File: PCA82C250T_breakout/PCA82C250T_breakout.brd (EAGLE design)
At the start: 36.8 x 17.8 mm, 11 parts, among them J1 RJ11

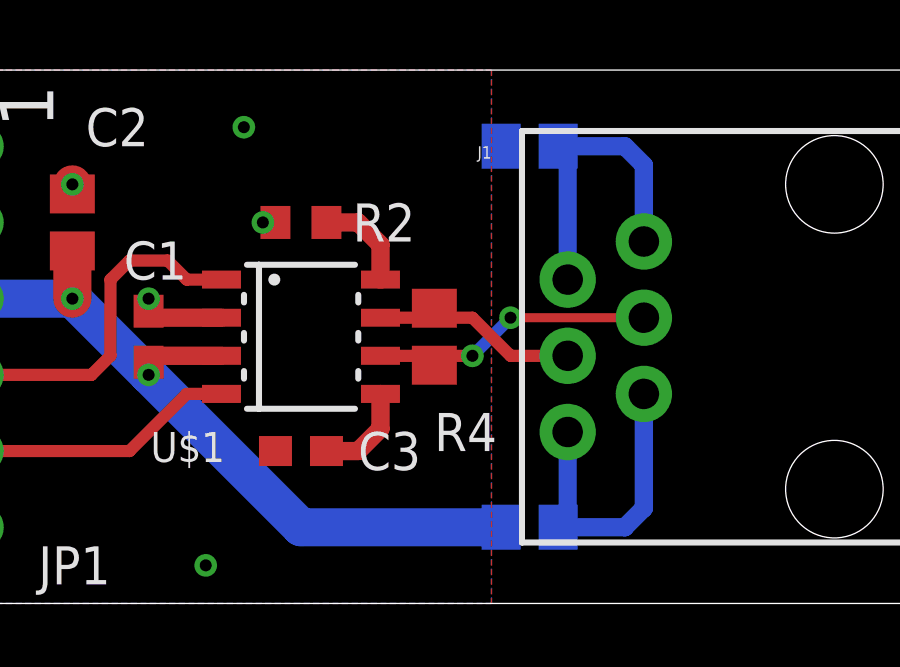
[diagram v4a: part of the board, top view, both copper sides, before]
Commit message: * small modifications and changed pinout
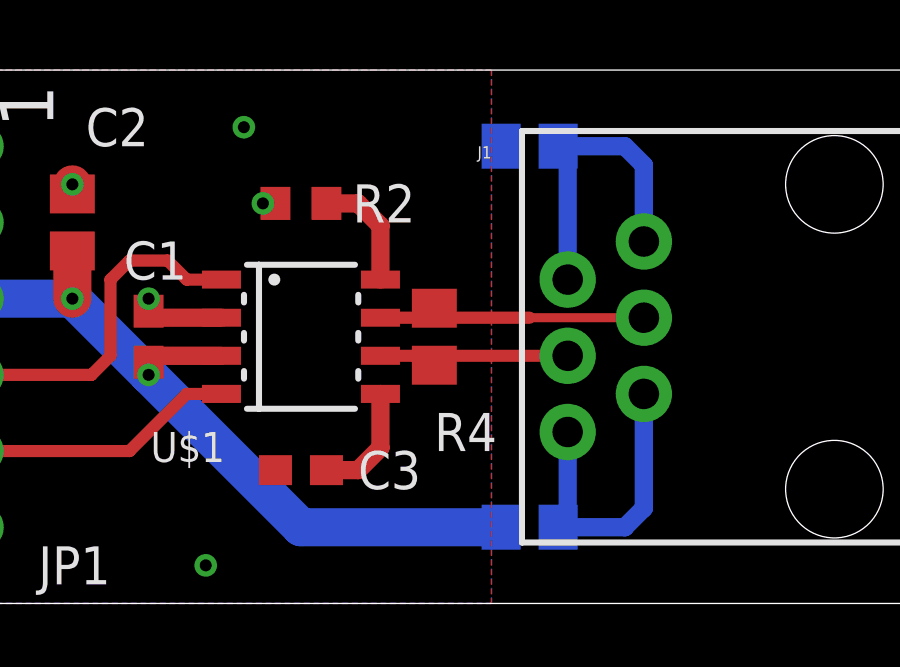
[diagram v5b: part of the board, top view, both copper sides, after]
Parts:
- moved R2 0.64 mm to (14.0, 13.3)
- moved C3 0.63 mm to (14.0, 4.45)
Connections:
- net CANH: now also J1.4; no longer J1.3
- net CANL: now also J1.3; no longer J1.4
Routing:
- net CANL: track 9.62 -> 6.55 mm, vias 2 -> 0
- net CANH: track 7.08 -> 9.04 mm
- net N$5: track 3.27 -> 3.90 mm
- net N$2: track 3.27 -> 3.90 mm
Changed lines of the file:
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@@
 <attribute name="VALUE" x="17.145" y="4.445" size="1.27" layer="28" rot="MR180"/>
 </element>
-<element name="R2" library="SquantorRCL" package="R0603" value="RS" x="13.97" y="12.7" smashed="yes" rot="R180">
-<attribute name="NAME" x="17.78" y="13.335" size="1.27" layer="25" rot="R180"/>
-<attribute name="VALUE" x="17.78" y="15.24" size="1.27" layer="27" rot="R180"/>
+<element name="R2" library="SquantorRCL" package="R0603" value="RS" x="13.97" y="13.335" smashed="yes" rot="R180">
+<attribute name="NAME" x="17.78" y="13.97" size="1.27" layer="25" rot="R180"/>
+<attribute name="VALUE" x="17.78" y="15.875" size="1.27" layer="27" rot="R180"/>
 </element>
-<element name="C3" library="SquantorRCL" package="C0603" value="DNS" x="13.97" y="5.08" smashed="yes">
-<attribute name="NAME" x="15.875" y="4.445" size="1.27" layer="25"/>
-<attribute name="VALUE" x="15.875" y="2.54" size="1.27" layer="27"/>
+<element name="C3" library="SquantorRCL" package="C0603" value="DNS" x="13.97" y="4.445" smashed="yes">
+<attribute name="NAME" x="15.875" y="3.81" size="1.27" layer="25"/>
+<attribute name="VALUE" x="15.875" y="1.905" size="1.27" layer="27"/>
 </element>
 <element name="R3" library="SquantorRCL" package="R0805" value="FB" x="21.59" y="15.24" smashed="yes" rot="MR180">
@@
 <via x="6.35" y="13.97" extent="1-16" drill="0.4" shape="octagon"/>
 <via x="8.89" y="10.16" extent="1-16" drill="0.4" shape="octagon"/>
-<via x="12.7" y="12.7" extent="1-16" drill="0.4" shape="octagon"/>
+<via x="12.7" y="13.335" extent="1-16" drill="0.4" shape="octagon"/>
 <wire x1="6.35" y1="13.65" x2="6.35" y2="13.97" width="1.27" layer="1"/>
 <wire x1="8.89" y1="10.16" x2="8.89" y2="9.74" width="0.6096" layer="1"/>
@@
 <contactref element="R2" pad="1"/>
 <contactref element="U$1" pad="8"/>
-<wire x1="16.62" y1="10.795" x2="16.62" y2="11.955" width="0.6096" layer="1"/>
-<wire x1="16.62" y1="11.955" x2="15.875" y2="12.7" width="0.6096" layer="1"/>
-<wire x1="15.875" y1="12.7" x2="14.82" y2="12.7" width="0.6096" layer="1"/>
+<wire x1="16.62" y1="10.795" x2="16.62" y2="12.59" width="0.6096" layer="1"/>
+<wire x1="16.62" y1="12.59" x2="15.875" y2="13.335" width="0.6096" layer="1"/>
+<wire x1="15.875" y1="13.335" x2="14.82" y2="13.335" width="0.6096" layer="1"/>
 </signal>
 <signal name="CANH">
 <contactref element="U$1" pad="7"/>
-<contactref element="J1" pad="3"/>
 <contactref element="R4" pad="2"/>
-<wire x1="16.62" y1="9.525" x2="18.415" y2="9.525" width="0.4064" layer="1"/>
-<wire x1="18.415" y1="9.525" x2="18.415" y2="9.84" width="0.4064" layer="1"/>
-<wire x1="18.415" y1="9.525" x2="19.685" y2="9.525" width="0.4064" layer="1"/>
-<wire x1="19.685" y1="9.525" x2="20.955" y2="8.255" width="0.4064" layer="1"/>
-<wire x1="20.955" y1="8.255" x2="22.86" y2="8.255" width="0.4064" layer="1"/>
+<contactref element="J1" pad="4"/>
+<wire x1="16.62" y1="9.525" x2="18.1" y2="9.525" width="0.4064" layer="1"/>
+<wire x1="18.1" y1="9.525" x2="18.415" y2="9.84" width="0.4064" layer="1"/>
+<wire x1="18.415" y1="9.84" x2="18.73" y2="9.525" width="0.4064" layer="1"/>
+<wire x1="18.73" y1="9.525" x2="21.59" y2="9.525" width="0.4064" layer="1"/>
+<wire x1="21.59" y1="9.525" x2="25.4" y2="9.525" width="0.3048" layer="1"/>
 </signal>
 <signal name="CANL">
 <contactref element="U$1" pad="6"/>
-<contactref element="J1" pad="4"/>
 <contactref element="R4" pad="1"/>
+<contactref element="J1" pad="3"/>
 <wire x1="16.62" y1="8.255" x2="18.415" y2="8.255" width="0.4064" layer="1"/>
-<wire x1="18.415" y1="8.255" x2="18.415" y2="7.94" width="0.4064" layer="1"/>
-<wire x1="18.415" y1="8.255" x2="19.685" y2="8.255" width="0.4064" layer="1"/>
-<via x="19.685" y="8.255" extent="1-16" drill="0.4" shape="octagon"/>
-<wire x1="19.685" y1="8.255" x2="20.955" y2="9.525" width="0.4064" layer="16"/>
-<via x="20.955" y="9.525" extent="1-16" drill="0.4" shape="octagon"/>
-<wire x1="25.4" y1="9.525" x2="20.955" y2="9.525" width="0.3048" layer="1"/>
+<wire x1="18.415" y1="8.255" x2="22.86" y2="8.255" width="0.4064" layer="1"/>
+<wire x1="18.415" y1="7.94" x2="18.415" y2="8.255" width="0.4064" layer="1"/>
 </signal>
 <signal name="N$2">
 <contactref element="U$1" pad="5"/>
 <contactref element="C3" pad="2"/>
-<wire x1="16.62" y1="6.985" x2="16.62" y2="5.825" width="0.6096" layer="1"/>
-<wire x1="16.62" y1="5.825" x2="15.875" y2="5.08" width="0.6096" layer="1"/>
-<wire x1="15.875" y1="5.08" x2="14.82" y2="5.08" width="0.6096" layer="1"/>
+<wire x1="16.62" y1="6.985" x2="16.62" y2="5.19" width="0.6096" layer="1"/>
+<wire x1="16.62" y1="5.19" x2="15.875" y2="4.445" width="0.6096" layer="1"/>
+<wire x1="15.875" y1="4.445" x2="14.82" y2="4.445" width="0.6096" layer="1"/>
 </signal>
 <signal name="UART_TX">

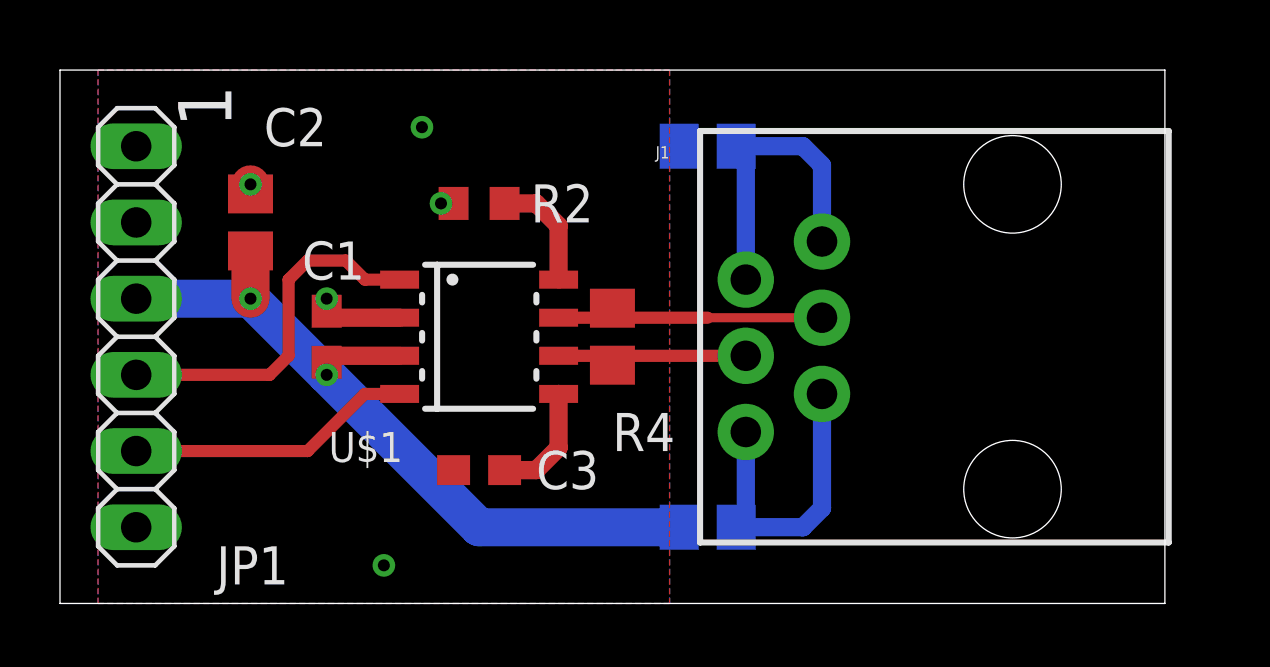
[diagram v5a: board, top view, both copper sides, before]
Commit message: * modified ISO 11898 termination to split termination to support stub connections.
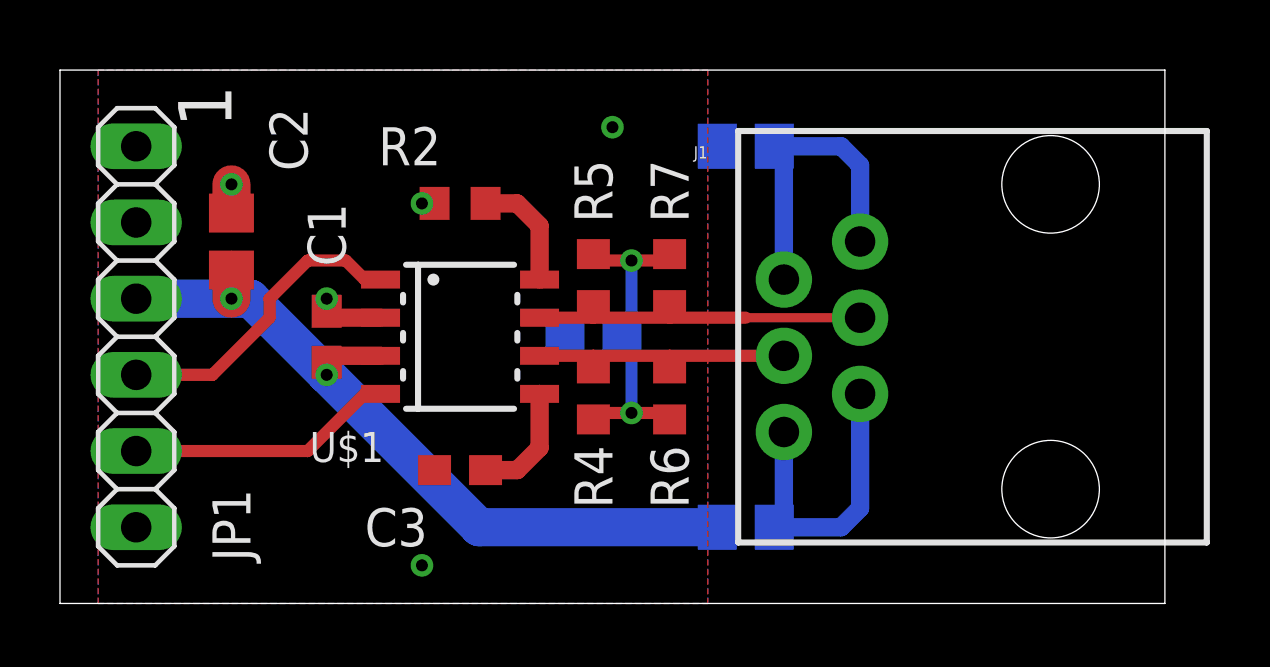
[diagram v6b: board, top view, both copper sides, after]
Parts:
- added C4: 10n, SquantorRCL:C0805
- added R5, R6, R7: 120, SquantorRCL:R0603
- R4: value 124 -> 120; device SquantorRCL:R0805 -> SquantorRCL:R0603
- moved R4 2.01 mm to (17.8, 6.99)
- moved J1 1.27 mm to (33.0, 8.89)
- moved LOGO1 1.27 mm to (15.2, 6.35)
- moved R1 1.27 mm to (22.9, 2.54)
- moved R3 1.27 mm to (22.9, 15.2)
- moved C2 0.90 mm to (5.71, 12.1)
- moved C3 0.63 mm to (13.3, 4.45)
- moved R2 0.63 mm to (13.3, 13.3)
- moved U$1 0.63 mm to (13.3, 8.89)
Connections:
- new net N$4: C4.1, R4.1, R5.2, R6.1, R7.2
- net CANH: now also R5.1, R7.1; no longer R4.2
- net CANL: now also R4.2, R6.2; no longer R4.1
- net GND: now also C4.2
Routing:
- net N$4: track 0.00 -> 11.3 mm, vias 0 -> 2
- net CANH: track 9.04 -> 11.5 mm
- net CANL: track 6.55 -> 8.99 mm
- net UART_TX: track 12.1 -> 10.4 mm
- net UART_RX: track 9.57 -> 8.93 mm
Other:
- board text added: "V2015.10.05"
- board text removed: "V2015.10.03"
